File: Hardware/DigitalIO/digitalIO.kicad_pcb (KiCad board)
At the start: 4 copper layers, 70 x 66.8 mm, 2 parts, among them J1 Conn_02x23_Odd_Even, J3 Conn_02x23_Odd_Even

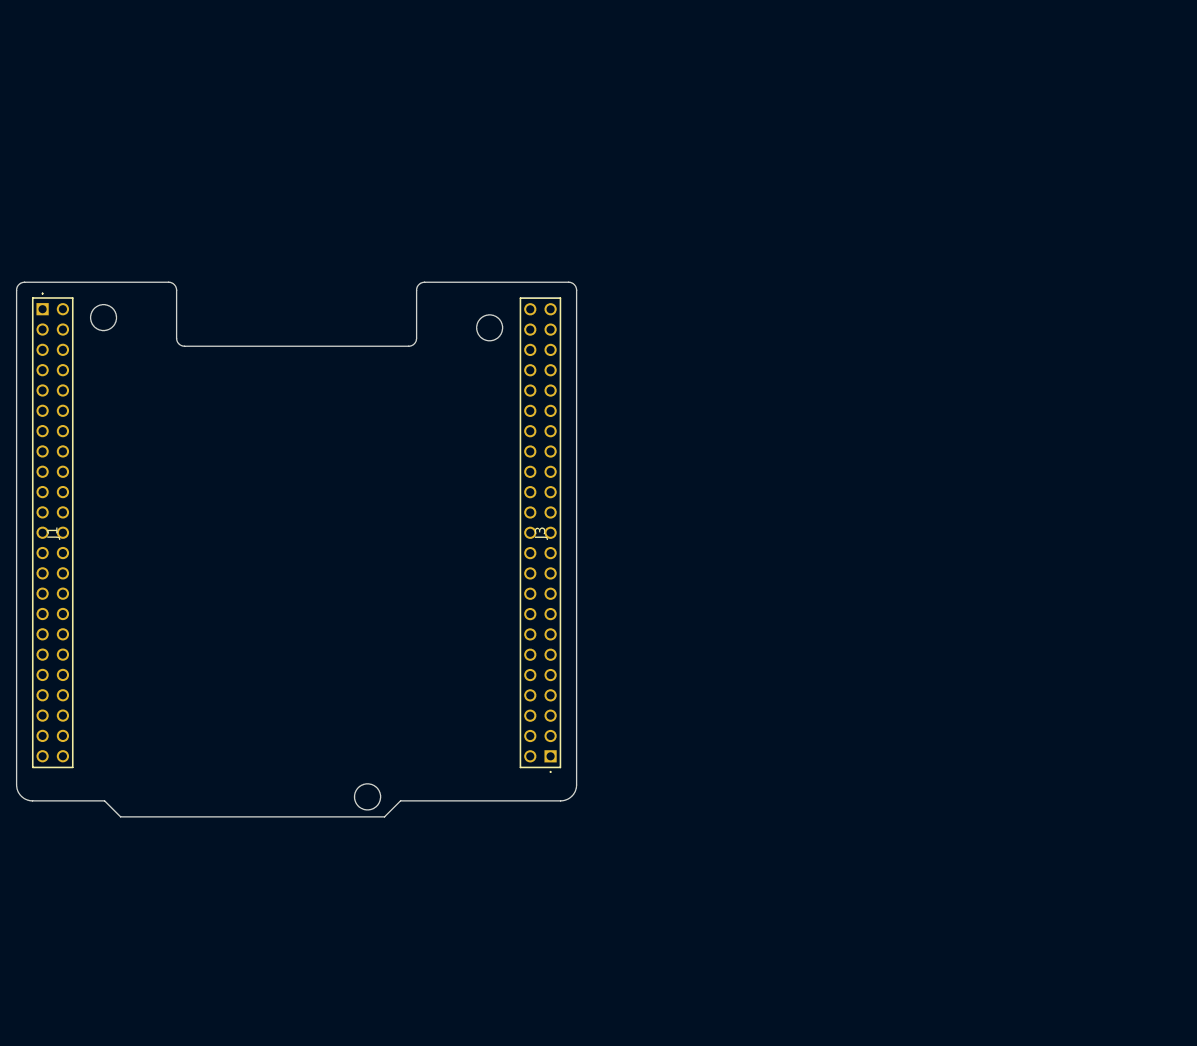
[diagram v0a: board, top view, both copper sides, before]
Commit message: schematic update - digital and analog footprints added
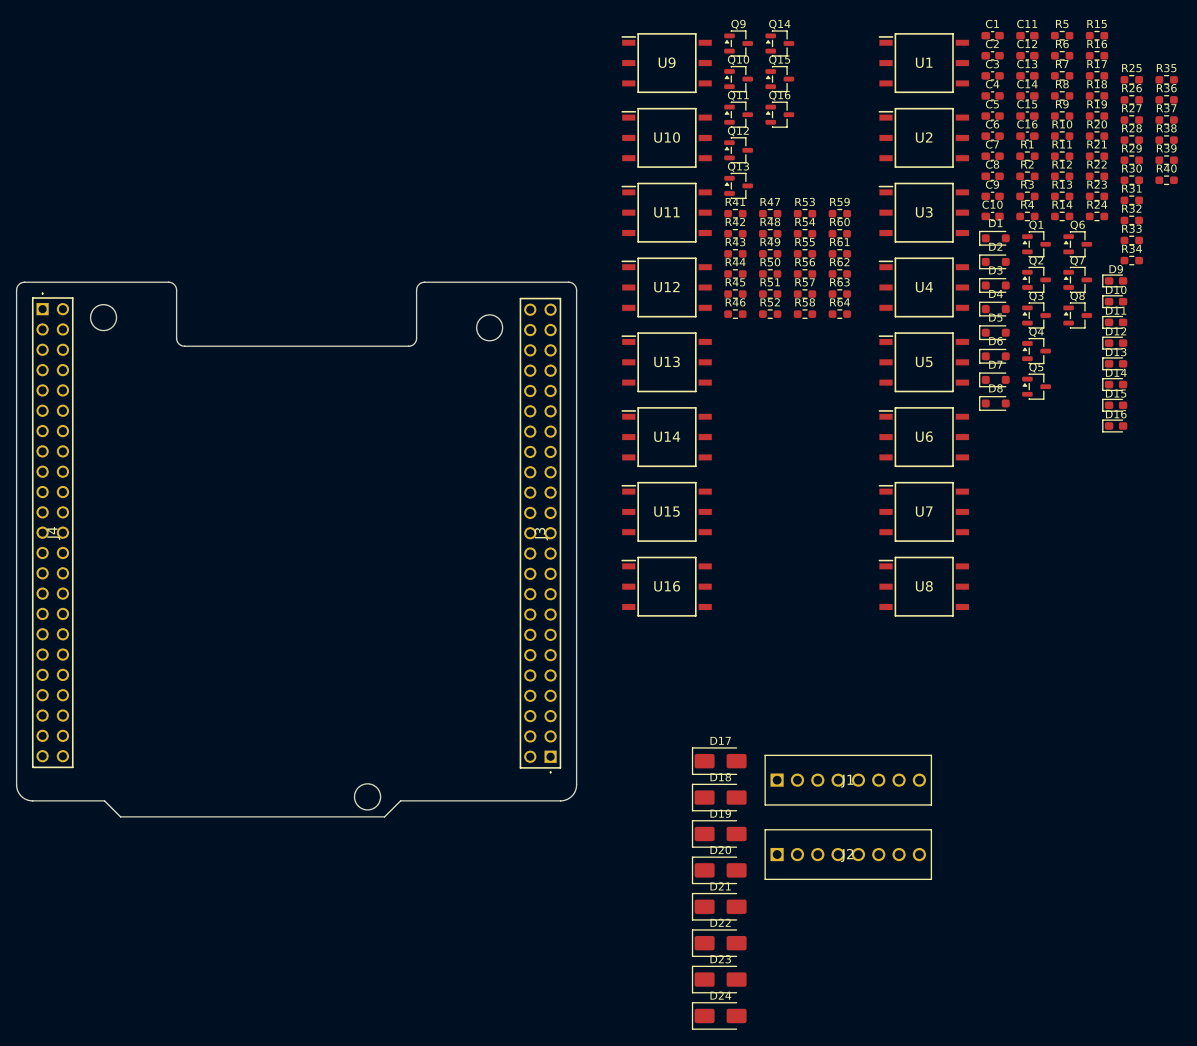
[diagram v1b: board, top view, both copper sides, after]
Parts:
- added C1: 1n, Capacitor_SMD:C_0603_1608Metric_Pad1.08x0.95mm_HandSolder, F.Cu at (238.0, 18.3)
- added C10: 470p, Capacitor_SMD:C_0603_1608Metric_Pad1.08x0.95mm_HandSolder, F.Cu at (238.0, 40.9)
- added C11: 470p, Capacitor_SMD:C_0603_1608Metric_Pad1.08x0.95mm_HandSolder, F.Cu at (242.3, 18.3)
- added C12: 470p, Capacitor_SMD:C_0603_1608Metric_Pad1.08x0.95mm_HandSolder, F.Cu at (242.3, 20.8)
- added C13: 470p, Capacitor_SMD:C_0603_1608Metric_Pad1.08x0.95mm_HandSolder, F.Cu at (242.3, 23.3)
- added C14: 470p, Capacitor_SMD:C_0603_1608Metric_Pad1.08x0.95mm_HandSolder, F.Cu at (242.3, 25.8)
- added C15: 470p, Capacitor_SMD:C_0603_1608Metric_Pad1.08x0.95mm_HandSolder, F.Cu at (242.3, 28.3)
- added C16: 470p, Capacitor_SMD:C_0603_1608Metric_Pad1.08x0.95mm_HandSolder, F.Cu at (242.3, 30.8)
- added C2: 1n, Capacitor_SMD:C_0603_1608Metric_Pad1.08x0.95mm_HandSolder, F.Cu at (238.0, 20.8)
- added C3: 1n, Capacitor_SMD:C_0603_1608Metric_Pad1.08x0.95mm_HandSolder, F.Cu at (238.0, 23.3)
- added C4: 1n, Capacitor_SMD:C_0603_1608Metric_Pad1.08x0.95mm_HandSolder, F.Cu at (238.0, 25.8)
- added C5: 1n, Capacitor_SMD:C_0603_1608Metric_Pad1.08x0.95mm_HandSolder, F.Cu at (238.0, 28.3)
- added C6: 1n, Capacitor_SMD:C_0603_1608Metric_Pad1.08x0.95mm_HandSolder, F.Cu at (238.0, 30.8)
- added C7: 1n, Capacitor_SMD:C_0603_1608Metric_Pad1.08x0.95mm_HandSolder, F.Cu at (238.0, 33.3)
- added C8: 1n, Capacitor_SMD:C_0603_1608Metric_Pad1.08x0.95mm_HandSolder, F.Cu at (238.0, 35.8)
- added C9: 470p, Capacitor_SMD:C_0603_1608Metric_Pad1.08x0.95mm_HandSolder, F.Cu at (238.0, 38.4)
- added D1: BZX384-B9V1, Diode_SMD:D_SOD-323_HandSoldering, F.Cu at (238.4, 43.6)
- added D10: LD_DI, LED_SMD:LED_0603_1608Metric_Pad1.05x0.95mm_HandSolder, F.Cu at (253.4, 51.5)
- added D11: LD_DI, LED_SMD:LED_0603_1608Metric_Pad1.05x0.95mm_HandSolder, F.Cu at (253.4, 54.1)
- added D12: LD_DI, LED_SMD:LED_0603_1608Metric_Pad1.05x0.95mm_HandSolder, F.Cu at (253.4, 56.7)
- added D13: LD_DI, LED_SMD:LED_0603_1608Metric_Pad1.05x0.95mm_HandSolder, F.Cu at (253.4, 59.3)
- added D14: LD_DI, LED_SMD:LED_0603_1608Metric_Pad1.05x0.95mm_HandSolder, F.Cu at (253.4, 61.9)
- added D15: LD_DI, LED_SMD:LED_0603_1608Metric_Pad1.05x0.95mm_HandSolder, F.Cu at (253.4, 64.5)
- added D16: LD_DI, LED_SMD:LED_0603_1608Metric_Pad1.05x0.95mm_HandSolder, F.Cu at (253.4, 67.1)
- added D17: SMA6L28A, Diode_SMD:D_SMA, F.Cu at (204.0, 109.0)
- added D18: SMA6L28A, Diode_SMD:D_SMA, F.Cu at (204.0, 113.5)
- added D19: SMA6L28A, Diode_SMD:D_SMA, F.Cu at (204.0, 118.0)
- added D2: BZX384-B9V1, Diode_SMD:D_SOD-323_HandSoldering, F.Cu at (238.4, 46.5)
- added D20: SMA6L28A, Diode_SMD:D_SMA, F.Cu at (204.0, 122.6)
- added D21: SMA6L28A, Diode_SMD:D_SMA, F.Cu at (204.0, 127.2)
- added D22: SMA6L28A, Diode_SMD:D_SMA, F.Cu at (204.0, 131.7)
- added D23: SMA6L28A, Diode_SMD:D_SMA, F.Cu at (204.0, 136.2)
- added D24: SMA6L28A, Diode_SMD:D_SMA, F.Cu at (204.0, 140.8)
- added D3: BZX384-B9V1, Diode_SMD:D_SOD-323_HandSoldering, F.Cu at (238.4, 49.5)
- added D4: BZX384-B9V1, Diode_SMD:D_SOD-323_HandSoldering, F.Cu at (238.4, 52.4)
- added D5: BZX384-B9V1, Diode_SMD:D_SOD-323_HandSoldering, F.Cu at (238.4, 55.4)
- added D6: BZX384-B9V1, Diode_SMD:D_SOD-323_HandSoldering, F.Cu at (238.4, 58.3)
- added D7: BZX384-B9V1, Diode_SMD:D_SOD-323_HandSoldering, F.Cu at (238.4, 61.3)
- added D8: BZX384-B9V1, Diode_SMD:D_SOD-323_HandSoldering, F.Cu at (238.4, 64.2)
- added D9: LD_DI, LED_SMD:LED_0603_1608Metric_Pad1.05x0.95mm_HandSolder, F.Cu at (253.4, 48.9)
- added J2: DIGITAL OUTPUT, PLC_STM:1725711, F.Cu at (211.1, 120.6)
- added J4: Conn_02x23_Odd_Even, PLC_STM:PRT12790, F.Cu at (119.2, 52.5)
- added Q1: SI2347DS, Package_TO_SOT_SMD:SOT-23-3, F.Cu at (243.5, 44.3)
- added Q10: SI2347DS, Package_TO_SOT_SMD:SOT-23-3, F.Cu at (206.2, 23.7)
- added Q11: SI2347DS, Package_TO_SOT_SMD:SOT-23-3, F.Cu at (206.2, 28.1)
- added Q12: SI2347DS, Package_TO_SOT_SMD:SOT-23-3, F.Cu at (206.2, 32.6)
- added Q13: SI2347DS, Package_TO_SOT_SMD:SOT-23-3, F.Cu at (206.2, 37.0)
- added Q14: SI2347DS, Package_TO_SOT_SMD:SOT-23-3, F.Cu at (211.4, 19.2)
- added Q15: SI2347DS, Package_TO_SOT_SMD:SOT-23-3, F.Cu at (211.4, 23.7)
- added Q16: SI2347DS, Package_TO_SOT_SMD:SOT-23-3, F.Cu at (211.4, 28.1)
- added Q2: SI2347DS, Package_TO_SOT_SMD:SOT-23-3, F.Cu at (243.5, 48.8)
- added Q3: SI2347DS, Package_TO_SOT_SMD:SOT-23-3, F.Cu at (243.5, 53.2)
- added Q4: SI2347DS, Package_TO_SOT_SMD:SOT-23-3, F.Cu at (243.5, 57.7)
- added Q5: SI2347DS, Package_TO_SOT_SMD:SOT-23-3, F.Cu at (243.5, 62.1)
- added Q6: SI2347DS, Package_TO_SOT_SMD:SOT-23-3, F.Cu at (248.6, 44.3)
- added Q7: SI2347DS, Package_TO_SOT_SMD:SOT-23-3, F.Cu at (248.6, 48.8)
- added Q8: SI2347DS, Package_TO_SOT_SMD:SOT-23-3, F.Cu at (248.6, 53.2)
- added Q9: SI2347DS, Package_TO_SOT_SMD:SOT-23-3, F.Cu at (206.2, 19.2)
- added R1: 47k, Resistor_SMD:R_0603_1608Metric_Pad0.98x0.95mm_HandSolder, F.Cu at (242.3, 33.3)
- added R10: 1k, Resistor_SMD:R_0603_1608Metric_Pad0.98x0.95mm_HandSolder, F.Cu at (246.7, 30.8)
- added R11: 1k, Resistor_SMD:R_0603_1608Metric_Pad0.98x0.95mm_HandSolder, F.Cu at (246.7, 33.3)
- added R12: 1k, Resistor_SMD:R_0603_1608Metric_Pad0.98x0.95mm_HandSolder, F.Cu at (246.7, 35.8)
- added R13: 1k, Resistor_SMD:R_0603_1608Metric_Pad0.98x0.95mm_HandSolder, F.Cu at (246.7, 38.4)
- added R14: 1k, Resistor_SMD:R_0603_1608Metric_Pad0.98x0.95mm_HandSolder, F.Cu at (246.7, 40.9)
- added R15: 1k, Resistor_SMD:R_0603_1608Metric_Pad0.98x0.95mm_HandSolder, F.Cu at (251.1, 18.3)
- added R16: 1k, Resistor_SMD:R_0603_1608Metric_Pad0.98x0.95mm_HandSolder, F.Cu at (251.1, 20.8)
- added R17: 270k, Resistor_SMD:R_0603_1608Metric_Pad0.98x0.95mm_HandSolder, F.Cu at (251.1, 23.3)
- added R18: 270k, Resistor_SMD:R_0603_1608Metric_Pad0.98x0.95mm_HandSolder, F.Cu at (251.1, 25.8)
- added R19: 270k, Resistor_SMD:R_0603_1608Metric_Pad0.98x0.95mm_HandSolder, F.Cu at (251.1, 28.3)
- added R2: 47k, Resistor_SMD:R_0603_1608Metric_Pad0.98x0.95mm_HandSolder, F.Cu at (242.3, 35.8)
- added R20: 270k, Resistor_SMD:R_0603_1608Metric_Pad0.98x0.95mm_HandSolder, F.Cu at (251.1, 30.8)
- added R21: 270k, Resistor_SMD:R_0603_1608Metric_Pad0.98x0.95mm_HandSolder, F.Cu at (251.1, 33.3)
- added R22: 270k, Resistor_SMD:R_0603_1608Metric_Pad0.98x0.95mm_HandSolder, F.Cu at (251.1, 35.8)
- added R23: 270k, Resistor_SMD:R_0603_1608Metric_Pad0.98x0.95mm_HandSolder, F.Cu at (251.1, 38.4)
- added R24: 270k, Resistor_SMD:R_0603_1608Metric_Pad0.98x0.95mm_HandSolder, F.Cu at (251.1, 40.9)
- added R25: 220R, Resistor_SMD:R_0603_1608Metric_Pad0.98x0.95mm_HandSolder, F.Cu at (255.4, 23.8)
- added R26: 1k, Resistor_SMD:R_0603_1608Metric_Pad0.98x0.95mm_HandSolder, F.Cu at (255.4, 26.3)
- added R27: 1k, Resistor_SMD:R_0603_1608Metric_Pad0.98x0.95mm_HandSolder, F.Cu at (255.4, 28.8)
- added R28: 1k, Resistor_SMD:R_0603_1608Metric_Pad0.98x0.95mm_HandSolder, F.Cu at (255.4, 31.3)
- added R29: 1k, Resistor_SMD:R_0603_1608Metric_Pad0.98x0.95mm_HandSolder, F.Cu at (255.4, 33.8)
- added R3: 47k, Resistor_SMD:R_0603_1608Metric_Pad0.98x0.95mm_HandSolder, F.Cu at (242.3, 38.4)
- added R30: 1k, Resistor_SMD:R_0603_1608Metric_Pad0.98x0.95mm_HandSolder, F.Cu at (255.4, 36.3)
- added R31: 1k, Resistor_SMD:R_0603_1608Metric_Pad0.98x0.95mm_HandSolder, F.Cu at (255.4, 38.8)
- added R32: 1k, Resistor_SMD:R_0603_1608Metric_Pad0.98x0.95mm_HandSolder, F.Cu at (255.4, 41.4)
- added R33: 1k, Resistor_SMD:R_0603_1608Metric_Pad0.98x0.95mm_HandSolder, F.Cu at (255.4, 43.9)
- added R34: 220R, Resistor_SMD:R_0603_1608Metric_Pad0.98x0.95mm_HandSolder, F.Cu at (255.4, 46.4)
- added R35: 220R, Resistor_SMD:R_0603_1608Metric_Pad0.98x0.95mm_HandSolder, F.Cu at (259.8, 23.8)
- added R36: 220R, Resistor_SMD:R_0603_1608Metric_Pad0.98x0.95mm_HandSolder, F.Cu at (259.8, 26.3)
- added R37: 220R, Resistor_SMD:R_0603_1608Metric_Pad0.98x0.95mm_HandSolder, F.Cu at (259.8, 28.8)
- added R38: 220R, Resistor_SMD:R_0603_1608Metric_Pad0.98x0.95mm_HandSolder, F.Cu at (259.8, 31.3)
- added R39: 220R, Resistor_SMD:R_0603_1608Metric_Pad0.98x0.95mm_HandSolder, F.Cu at (259.8, 33.8)
- added R4: 47k, Resistor_SMD:R_0603_1608Metric_Pad0.98x0.95mm_HandSolder, F.Cu at (242.3, 40.9)
- added R40: 220R, Resistor_SMD:R_0603_1608Metric_Pad0.98x0.95mm_HandSolder, F.Cu at (259.8, 36.3)
- added R41: 47k, Resistor_SMD:R_0603_1608Metric_Pad0.98x0.95mm_HandSolder, F.Cu at (205.8, 40.5)
- added R42: 47k, Resistor_SMD:R_0603_1608Metric_Pad0.98x0.95mm_HandSolder, F.Cu at (205.8, 43.0)
- added R43: 47k, Resistor_SMD:R_0603_1608Metric_Pad0.98x0.95mm_HandSolder, F.Cu at (205.8, 45.5)
- added R44: 47k, Resistor_SMD:R_0603_1608Metric_Pad0.98x0.95mm_HandSolder, F.Cu at (205.8, 48.0)
- added R45: 47k, Resistor_SMD:R_0603_1608Metric_Pad0.98x0.95mm_HandSolder, F.Cu at (205.8, 50.6)
- added R46: 47k, Resistor_SMD:R_0603_1608Metric_Pad0.98x0.95mm_HandSolder, F.Cu at (205.8, 53.1)
- added R47: 47k, Resistor_SMD:R_0603_1608Metric_Pad0.98x0.95mm_HandSolder, F.Cu at (210.2, 40.5)
- added R48: 47k, Resistor_SMD:R_0603_1608Metric_Pad0.98x0.95mm_HandSolder, F.Cu at (210.2, 43.0)
- added R49: 1k, Resistor_SMD:R_0603_1608Metric_Pad0.98x0.95mm_HandSolder, F.Cu at (210.2, 45.5)
- added R5: 47k, Resistor_SMD:R_0603_1608Metric_Pad0.98x0.95mm_HandSolder, F.Cu at (246.7, 18.3)
- added R50: 1k, Resistor_SMD:R_0603_1608Metric_Pad0.98x0.95mm_HandSolder, F.Cu at (210.2, 48.0)
- added R51: 1k, Resistor_SMD:R_0603_1608Metric_Pad0.98x0.95mm_HandSolder, F.Cu at (210.2, 50.6)
- added R52: 1k, Resistor_SMD:R_0603_1608Metric_Pad0.98x0.95mm_HandSolder, F.Cu at (210.2, 53.1)
- added R53: 1k, Resistor_SMD:R_0603_1608Metric_Pad0.98x0.95mm_HandSolder, F.Cu at (214.6, 40.5)
- added R54: 1k, Resistor_SMD:R_0603_1608Metric_Pad0.98x0.95mm_HandSolder, F.Cu at (214.6, 43.0)
- added R55: 1k, Resistor_SMD:R_0603_1608Metric_Pad0.98x0.95mm_HandSolder, F.Cu at (214.6, 45.5)
- added R56: 1k, Resistor_SMD:R_0603_1608Metric_Pad0.98x0.95mm_HandSolder, F.Cu at (214.6, 48.0)
- added R57: 1k, Resistor_SMD:R_0603_1608Metric_Pad0.98x0.95mm_HandSolder, F.Cu at (214.6, 50.6)
- added R58: 1k, Resistor_SMD:R_0603_1608Metric_Pad0.98x0.95mm_HandSolder, F.Cu at (214.6, 53.1)
- added R59: 1k, Resistor_SMD:R_0603_1608Metric_Pad0.98x0.95mm_HandSolder, F.Cu at (218.9, 40.5)
- added R6: 47k, Resistor_SMD:R_0603_1608Metric_Pad0.98x0.95mm_HandSolder, F.Cu at (246.7, 20.8)
- added R60: 1k, Resistor_SMD:R_0603_1608Metric_Pad0.98x0.95mm_HandSolder, F.Cu at (218.9, 43.0)
- added R61: 1k, Resistor_SMD:R_0603_1608Metric_Pad0.98x0.95mm_HandSolder, F.Cu at (218.9, 45.5)
- added R62: 1k, Resistor_SMD:R_0603_1608Metric_Pad0.98x0.95mm_HandSolder, F.Cu at (218.9, 48.0)
- added R63: 1k, Resistor_SMD:R_0603_1608Metric_Pad0.98x0.95mm_HandSolder, F.Cu at (218.9, 50.6)
- added R64: 1k, Resistor_SMD:R_0603_1608Metric_Pad0.98x0.95mm_HandSolder, F.Cu at (218.9, 53.1)
- added R7: 47k, Resistor_SMD:R_0603_1608Metric_Pad0.98x0.95mm_HandSolder, F.Cu at (246.7, 23.3)
- added R8: 47k, Resistor_SMD:R_0603_1608Metric_Pad0.98x0.95mm_HandSolder, F.Cu at (246.7, 25.8)
- added R9: 1k, Resistor_SMD:R_0603_1608Metric_Pad0.98x0.95mm_HandSolder, F.Cu at (246.7, 28.3)
- added U1: CNY17-3, PLC_STM:SOP254P1016X400-6N, F.Cu at (229.4, 21.7)
- added U10: CNY17-3, PLC_STM:SOP254P1016X400-6N, F.Cu at (197.3, 31.0)
- added U11: CNY17-3, PLC_STM:SOP254P1016X400-6N, F.Cu at (197.3, 40.4)
- added U12: CNY17-3, PLC_STM:SOP254P1016X400-6N, F.Cu at (197.3, 49.7)
- added U13: CNY17-3, PLC_STM:SOP254P1016X400-6N, F.Cu at (197.3, 59.1)
- added U14: CNY17-3, PLC_STM:SOP254P1016X400-6N, F.Cu at (197.3, 68.4)
- added U15: CNY17-3, PLC_STM:SOP254P1016X400-6N, F.Cu at (197.3, 77.8)
- added U16: CNY17-3, PLC_STM:SOP254P1016X400-6N, F.Cu at (197.3, 87.1)
- added U2: CNY17-3, PLC_STM:SOP254P1016X400-6N, F.Cu at (229.4, 31.0)
- added U3: CNY17-3, PLC_STM:SOP254P1016X400-6N, F.Cu at (229.4, 40.4)
- added U4: CNY17-3, PLC_STM:SOP254P1016X400-6N, F.Cu at (229.4, 49.7)
- added U5: CNY17-3, PLC_STM:SOP254P1016X400-6N, F.Cu at (229.4, 59.1)
- added U6: CNY17-3, PLC_STM:SOP254P1016X400-6N, F.Cu at (229.4, 68.4)
- added U7: CNY17-3, PLC_STM:SOP254P1016X400-6N, F.Cu at (229.4, 77.8)
- added U8: CNY17-3, PLC_STM:SOP254P1016X400-6N, F.Cu at (229.4, 87.1)
- added U9: CNY17-3, PLC_STM:SOP254P1016X400-6N, F.Cu at (197.3, 21.7)
- J1: value Conn_02x23_Odd_Even -> DIGITAL INPUT; footprint PLC_STM_Power:PRT12790 -> PLC_STM:1725711
- J3: footprint PLC_STM_Power:PRT12790 -> PLC_STM:PRT12790
- moved J1 109.1 mm to (211.1, 111.3), turned to 0 degrees
- moved J3 0.06 mm to (182.8, 108.4)
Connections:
- J1 pad 1: unconnected-(J1-Pin_1-Pad1) -> /connectors/DI_IN0
- J1 pad 2: unconnected-(J1-Pin_2-Pad2) -> /connectors/DI_IN1
- J1 pad 3: unconnected-(J1-Pin_3-Pad3) -> /connectors/DI_IN2
- J1 pad 4: unconnected-(J1-Pin_4-Pad4) -> /connectors/DI_IN3
- J1 pad 5: unconnected-(J1-Pin_5-Pad5) -> /connectors/DI_IN4
- J1 pad 6: unconnected-(J1-Pin_6-Pad6) -> /connectors/DI_IN5
- J1 pad 7: unconnected-(J1-Pin_7-Pad7) -> /connectors/DI_IN6
- J1 pad 8: unconnected-(J1-Pin_8-Pad8) -> /connectors/DI_IN7
- J3 pad 10: unconnected-(J3-Pin_10-Pad10) -> UART5_TX
- J3 pad 11: unconnected-(J3-Pin_11-Pad11) -> GND
- J3 pad 12: unconnected-(J3-Pin_12-Pad12) -> UART5_RX
- J3 pad 13: unconnected-(J3-Pin_13-Pad13) -> GND
- J3 pad 15: unconnected-(J3-Pin_15-Pad15) -> VIN
- J3 pad 19: unconnected-(J3-Pin_19-Pad19) -> ANALOG_IN3
- J3 pad 21: unconnected-(J3-Pin_21-Pad21) -> ANALOG_IN10
- J3 pad 22: unconnected-(J3-Pin_22-Pad22) -> UART2_RX
- J3 pad 23: unconnected-(J3-Pin_23-Pad23) -> ANALOG_IN13
- J3 pad 24: unconnected-(J3-Pin_24-Pad24) -> UART2_TX
- J3 pad 25: unconnected-(J3-Pin_25-Pad25) -> ANALOG_IN3/9
- J3 pad 27: unconnected-(J3-Pin_27-Pad27) -> ANALOG_IN3/15
- J3 pad 29: unconnected-(J3-Pin_29-Pad29) -> ANALOG_IN3/8
- J3 pad 30: unconnected-(J3-Pin_30-Pad30) -> GND
- J3 pad 39: unconnected-(J3-Pin_39-Pad39) -> GND
- J3 pad 40: unconnected-(J3-Pin_40-Pad40) -> ANALOG_IN3/6
- J3 pad 41: unconnected-(J3-Pin_41-Pad41) -> CAN1_RX
- J3 pad 42: unconnected-(J3-Pin_42-Pad42) -> ANALOG_IN3/5
- J3 pad 43: unconnected-(J3-Pin_43-Pad43) -> CAN1_TX
- J3 pad 44: unconnected-(J3-Pin_44-Pad44) -> ANALOG_IN3/7
- J3 pad 6: unconnected-(J3-Pin_6-Pad6) -> UART4_TX
- J3 pad 7: unconnected-(J3-Pin_7-Pad7) -> 3V3
- J3 pad 8: unconnected-(J3-Pin_8-Pad8) -> UART4_RX
- J3 pad 9: unconnected-(J3-Pin_9-Pad9) -> 5V
